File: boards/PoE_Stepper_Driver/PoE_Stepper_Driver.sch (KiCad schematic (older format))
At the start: 4 parts

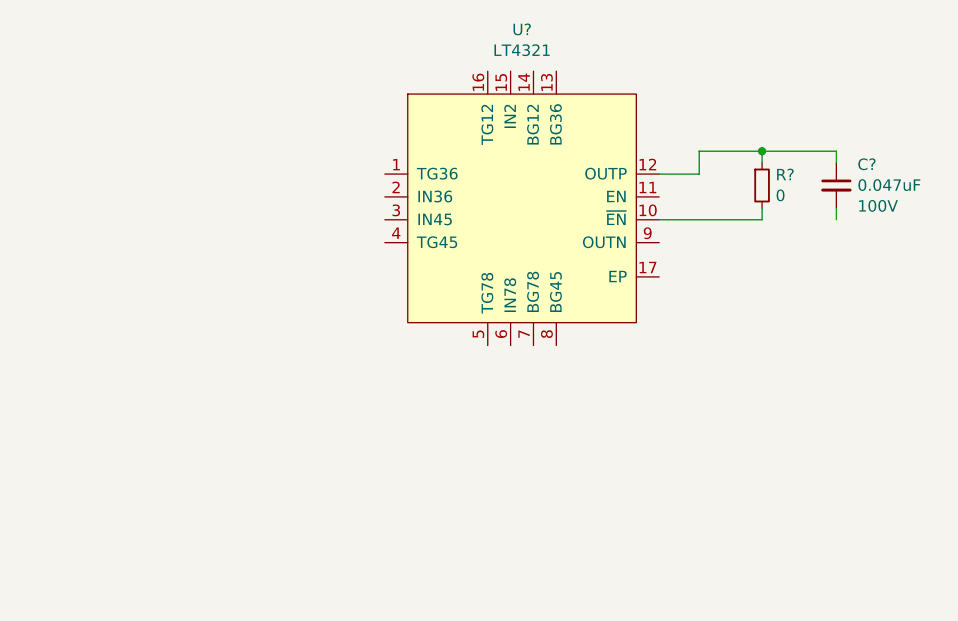
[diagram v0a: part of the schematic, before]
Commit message: started poe side of schematic
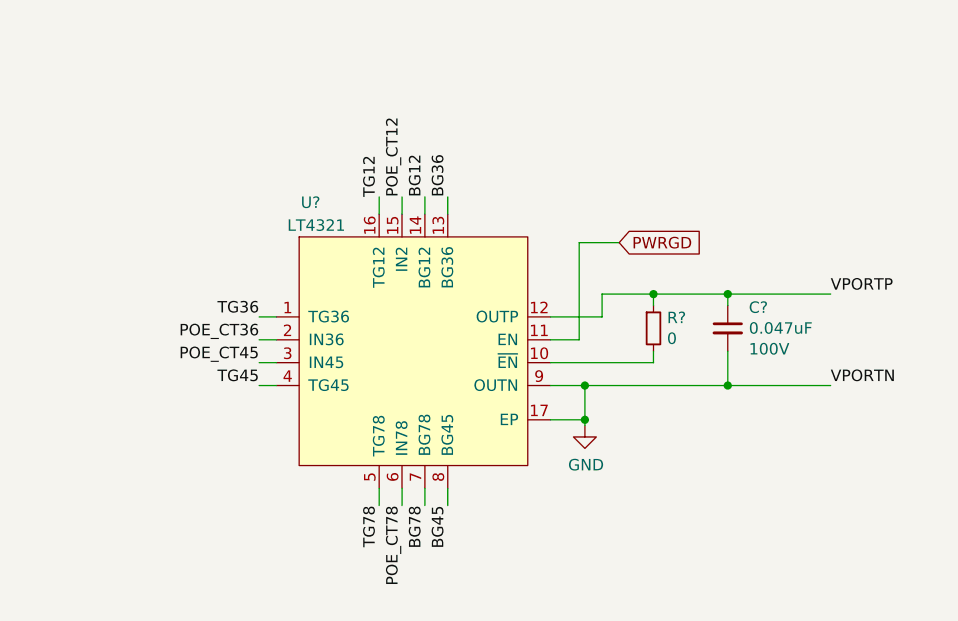
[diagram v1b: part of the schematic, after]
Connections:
- net labels added: BG12, BG36, BG45, BG78, GND, POE_CT12, POE_CT36, POE_CT45, POE_CT78, PWRGD, TG12, TG36, TG45, TG78, VPORTN, VPORTP
- wire segments 9 -> 31
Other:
- moved on the sheet: C?, R?, U?
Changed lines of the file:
@@
 L ECE445:LT4321 U?
 U 1 1 61FBDFD6
-P 6825 2875
-F 0 "U?" H 6825 3656 50  0000 C CNN
-F 1 "LT4321" H 6825 3565 50  0000 C CNN
-F 2 "" H 6475 3425 50  0001 C CNN
-F 3 "" H 6475 3425 50  0001 C CNN
-	1    6825 2875
+P 6350 3500
+F 0 "U?" H 5900 4150 50  0000 C CNN
+F 1 "LT4321" H 5925 4050 50  0000 C CNN
+F 2 "" H 6000 4050 50  0001 C CNN
+F 3 "" H 6000 4050 50  0001 C CNN
+	1    6350 3500
 	1    0    0    -1
 $EndComp
@@
 L device:C_Small C?
 U 1 1 61FBE7CA
-P 8200 2775
-F 0 "C?" H 8292 2866 50  0000 L CNN
-F 1 "0.047uF" H 8292 2775 50  0000 L CNN
-F 2 "" H 8200 2775 50  0001 C CNN
-F 3 "~" H 8200 2775 50  0001 C CNN
-F 4 "100V" H 8292 2684 50  0000 L CNN "Voltage"
-	1    8200 2775
+P 7725 3400
+F 0 "C?" H 7817 3491 50  0000 L CNN
+F 1 "0.047uF" H 7817 3400 50  0000 L CNN
+F 2 "" H 7725 3400 50  0001 C CNN
+F 3 "~" H 7725 3400 50  0001 C CNN
+F 4 "100V" H 7817 3309 50  0000 L CNN "Voltage"
+	1    7725 3400
 	1    0    0    -1
 $EndComp
 Wire Wire Line
-	8200 2625 8200 2675
-Wire Wire Line
-	8200 2925 8200 2875
+	7725 3250 7725 3300
 $Comp
 L device:R_Small R?
 U 1 1 61FC1A67
-P 7875 2775
-F 0 "R?" H 7934 2821 50  0000 L CNN
-F 1 "0" H 7934 2730 50  0000 L CNN
-F 2 "" H 7875 2775 50  0001 C CNN
-F 3 "~" H 7875 2775 50  0001 C CNN
-	1    7875 2775
+P 7400 3400
+F 0 "R?" H 7459 3446 50  0000 L CNN
+F 1 "0" H 7459 3355 50  0000 L CNN
+F 2 "" H 7400 3400 50  0001 C CNN
+F 3 "~" H 7400 3400 50  0001 C CNN
+	1    7400 3400
 	1    0    0    -1
 $EndComp
 Wire Wire Line
-	7875 2625 7875 2675
+	7400 3250 7400 3300
 Wire Wire Line
-	7875 2625 8200 2625
+	7400 3250 7725 3250
 Wire Wire Line
-	7875 2875 7875 2925
+	7400 3500 7400 3550
 Wire Wire Line
-	7875 2925 7425 2925
+	7400 3550 6950 3550
 Wire Wire Line
-	7425 2725 7600 2725
+	6950 3650 7100 3650
 Wire Wire Line
-	7600 2725 7600 2625
+	7725 3500 7725 3650
+Text GLabel 7250 3025 2    50   Input ~ 0
+PWRGD
 Wire Wire Line
-	7600 2625 7875 2625
-Connection ~ 7875 2625
+	6950 3450 7075 3450
+Wire Wire Line
+	7075 3450 7075 3025
+Wire Wire Line
+	7075 3025 7250 3025
+Wire Wire Line
+	7175 3350 7175 3250
+Wire Wire Line
+	7175 3250 7400 3250
+Wire Wire Line
+	6950 3350 7175 3350
+Connection ~ 7400 3250
+Text Label 6500 2825 1    50   ~ 0
+BG36
+Wire Wire Line
+	6500 2825 6500 2900
+Text Label 6400 2825 1    50   ~ 0
+BG12
+Wire Wire Line
+	6400 2825 6400 2900
+Text Label 6300 2825 1    50   ~ 0
+POE_CT12
+Wire Wire Line
+	6300 2825 6300 2900
+Text Label 6200 2825 1    50   ~ 0
+TG12
+Wire Wire Line
+	6200 2825 6200 2900
+Text Label 5675 3350 2    50   ~ 0
+TG36
+Wire Wire Line
+	5675 3350 5750 3350
+Text Label 5675 3450 2    50   ~ 0
+POE_CT36
+Wire Wire Line
+	5675 3450 5750 3450
+Text Label 5675 3550 2    50   ~ 0
+POE_CT45
+Wire Wire Line
+	5675 3550 5750 3550
+Text Label 5675 3650 2    50   ~ 0
+TG45
+Wire Wire Line
+	5675 3650 5750 3650
+Text Label 6200 4175 3    50   ~ 0
+TG78
+Wire Wire Line
+	6200 4175 6200 4100
+Text Label 6300 4175 3    50   ~ 0
+POE_CT78
+Wire Wire Line
+	6300 4175 6300 4100
+Text Label 6400 4175 3    50   ~ 0
+BG78
+Wire Wire Line
+	6400 4175 6400 4100
+Text Label 6500 4175 3    50   ~ 0
+BG45
+Wire Wire Line
+	6500 4175 6500 4100
+$Comp
+L power:GND #PWR?
+U 1 1 61FC94D9
+P 7100 3825
+F 0 "#PWR?" H 7100 3575 50  0001 C CNN
+F 1 "GND" H 7105 3652 50  0000 C CNN
+F 2 "" H 7100 3825 50  0001 C CNN
+F 3 "" H 7100 3825 50  0001 C CNN
+	1    7100 3825
+	1    0    0    -1
+$EndComp
+Wire Wire Line
+	6950 3800 7100 3800
+Wire Wire Line
+	7100 3800 7100 3825
+Wire Wire Line
+	7100 3650 7100 3800
+Connection ~ 7100 3650
+Wire Wire Line
+	7100 3650 7725 3650
+Connection ~ 7100 3800
+Text Label 8175 3250 0    50   ~ 0
+VPORTP
+Text Label 8175 3650 0    50   ~ 0
+VPORTN
+Wire Wire Line
+	7725 3250 8175 3250
+Connection ~ 7725 3250
+Wire Wire Line
+	7725 3650 8175 3650
+Connection ~ 7725 3650
 $EndSCHEMATC

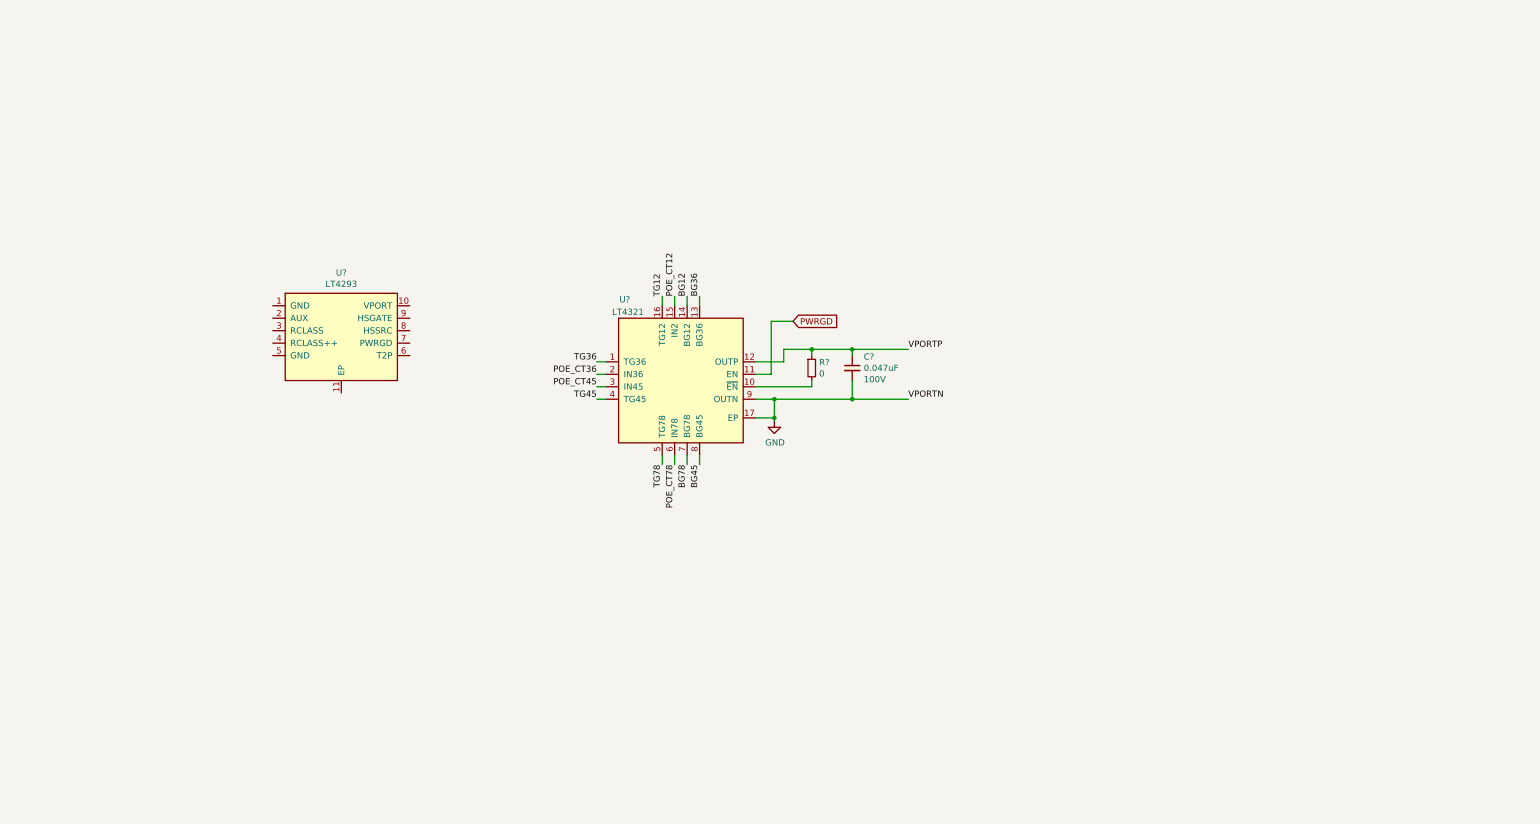
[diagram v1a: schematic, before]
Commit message: added ethernet transformer
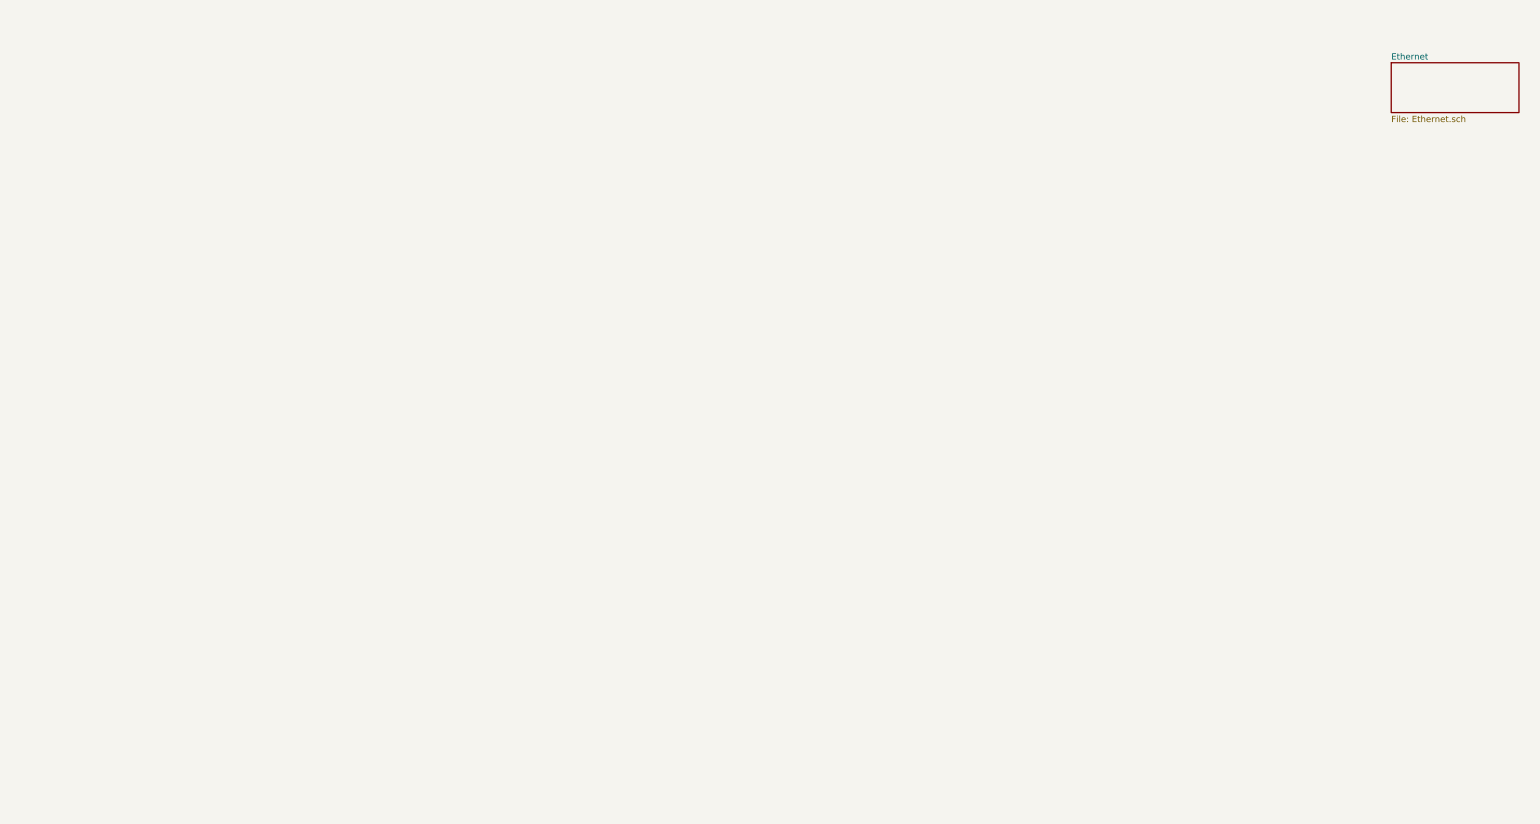
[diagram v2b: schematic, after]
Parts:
- removed C?: 0.047uF, symbol device:C_Small
- removed R?: 0, symbol device:R_Small
- removed U?: LT4293, symbol ECE445:LT4293
- removed U?: LT4321, symbol ECE445:LT4321
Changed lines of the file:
@@
 $Descr A4 11693 8268
 encoding utf-8
-Sheet 1 1
+Sheet 1 2
 Title ""
 Date ""
@@
 Comment4 ""
 $EndDescr
-$Comp
-L ECE445:LT4293 U?
-U 1 1 61FB857D
-P 3625 3100
-F 0 "U?" H 3625 3565 50  0000 C CNN
-F 1 "LT4293" H 3625 3474 50  0000 C CNN
-F 2 "" H 3475 3550 50  0001 C CNN
-F 3 "" H 3475 3550 50  0001 C CNN
-	1    3625 3100
-	1    0    0    -1
-$EndComp
-$Comp
-L ECE445:LT4321 U?
-U 1 1 61FBDFD6
-P 6350 3500
-F 0 "U?" H 5900 4150 50  0000 C CNN
-F 1 "LT4321" H 5925 4050 50  0000 C CNN
-F 2 "" H 6000 4050 50  0001 C CNN
-F 3 "" H 6000 4050 50  0001 C CNN
-	1    6350 3500
-	1    0    0    -1
-$EndComp
-$Comp
-L device:C_Small C?
-U 1 1 61FBE7CA
-P 7725 3400
-F 0 "C?" H 7817 3491 50  0000 L CNN
-F 1 "0.047uF" H 7817 3400 50  0000 L CNN
-F 2 "" H 7725 3400 50  0001 C CNN
-F 3 "~" H 7725 3400 50  0001 C CNN
-F 4 "100V" H 7817 3309 50  0000 L CNN "Voltage"
-	1    7725 3400
-	1    0    0    -1
-$EndComp
-Wire Wire Line
-	7725 3250 7725 3300
-$Comp
-L device:R_Small R?
-U 1 1 61FC1A67
-P 7400 3400
-F 0 "R?" H 7459 3446 50  0000 L CNN
-F 1 "0" H 7459 3355 50  0000 L CNN
-F 2 "" H 7400 3400 50  0001 C CNN
-F 3 "~" H 7400 3400 50  0001 C CNN
-	1    7400 3400
-	1    0    0    -1
-$EndComp
-Wire Wire Line
-	7400 3250 7400 3300
-Wire Wire Line
-	7400 3250 7725 3250
-Wire Wire Line
-	7400 3500 7400 3550
-Wire Wire Line
-	7400 3550 6950 3550
-Wire Wire Line
-	6950 3650 7100 3650
-Wire Wire Line
-	7725 3500 7725 3650
-Text GLabel 7250 3025 2    50   Input ~ 0
-PWRGD
-Wire Wire Line
-	6950 3450 7075 3450
-Wire Wire Line
-	7075 3450 7075 3025
-Wire Wire Line
-	7075 3025 7250 3025
-Wire Wire Line
-	7175 3350 7175 3250
-Wire Wire Line
-	7175 3250 7400 3250
-Wire Wire Line
-	6950 3350 7175 3350
-Connection ~ 7400 3250
-Text Label 6500 2825 1    50   ~ 0
-BG36
-Wire Wire Line
-	6500 2825 6500 2900
-Text Label 6400 2825 1    50   ~ 0
-BG12
-Wire Wire Line
-	6400 2825 6400 2900
-Text Label 6300 2825 1    50   ~ 0
-POE_CT12
-Wire Wire Line
-	6300 2825 6300 2900
-Text Label 6200 2825 1    50   ~ 0
-TG12
-Wire Wire Line
-	6200 2825 6200 2900
-Text Label 5675 3350 2    50   ~ 0
-TG36
-Wire Wire Line
-	5675 3350 5750 3350
-Text Label 5675 3450 2    50   ~ 0
-POE_CT36
-Wire Wire Line
-	5675 3450 5750 3450
-Text Label 5675 3550 2    50   ~ 0
-POE_CT45
-Wire Wire Line
-	5675 3550 5750 3550
-Text Label 5675 3650 2    50   ~ 0
-TG45
-Wire Wire Line
-	5675 3650 5750 3650
-Text Label 6200 4175 3    50   ~ 0
-TG78
-Wire Wire Line
-	6200 4175 6200 4100
-Text Label 6300 4175 3    50   ~ 0
-POE_CT78
-Wire Wire Line
-	6300 4175 6300 4100
-Text Label 6400 4175 3    50   ~ 0
-BG78
-Wire Wire Line
-	6400 4175 6400 4100
-Text Label 6500 4175 3    50   ~ 0
-BG45
-Wire Wire Line
-	6500 4175 6500 4100
-$Comp
-L power:GND #PWR?
-U 1 1 61FC94D9
-P 7100 3825
-F 0 "#PWR?" H 7100 3575 50  0001 C CNN
-F 1 "GND" H 7105 3652 50  0000 C CNN
-F 2 "" H 7100 3825 50  0001 C CNN
-F 3 "" H 7100 3825 50  0001 C CNN
-	1    7100 3825
-	1    0    0    -1
-$EndComp
-Wire Wire Line
-	6950 3800 7100 3800
-Wire Wire Line
-	7100 3800 7100 3825
-Wire Wire Line
-	7100 3650 7100 3800
-Connection ~ 7100 3650
-Wire Wire Line
-	7100 3650 7725 3650
-Connection ~ 7100 3800
-Text Label 8175 3250 0    50   ~ 0
-VPORTP
-Text Label 8175 3650 0    50   ~ 0
-VPORTN
-Wire Wire Line
-	7725 3250 8175 3250
-Connection ~ 7725 3250
-Wire Wire Line
-	7725 3650 8175 3650
-Connection ~ 7725 3650
+$Sheet
+S 12050 950  1025 400
+U 620ECB3C
+F0 "Ethernet" 50
+F1 "Ethernet.sch" 50
+$EndSheet
 $EndSCHEMATC

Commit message: added trinamic chips
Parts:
- added U?: STM32F107RBTx, Package_QFP:LQFP-64_10x10mm_P0.5mm, symbol MCU_ST_STM32F1:STM32F107RBTx
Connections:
- net labels added: PWRGD, VOUT+, VOUT-
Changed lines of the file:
@@
 $Descr A4 11693 8268
 encoding utf-8
-Sheet 1 2
+Sheet 1 3
 Title ""
 Date ""
@@
 F1 "Ethernet.sch" 50
 $EndSheet
+$Comp
+L MCU_ST_STM32F1:STM32F107RBTx U?
+U 1 1 6292DDC0
+P 6025 3225
+F 0 "U?" H 6025 1336 50  0000 C CNN
+F 1 "STM32F107RBTx" H 6025 1245 50  0000 C CNN
+F 2 "Package_QFP:LQFP-64_10x10mm_P0.5mm" H 5425 1525 50  0001 R CNN
+F 3 "http://www.st.com/st-web-ui/static/active/en/resource/technical/document/datasheet/CD00220364.pdf" H 6025 3225 50  0001 C CNN
+	1    6025 3225
+	1    0    0    -1
+$EndComp
+$Sheet
+S 12050 1575 1025 275
+U 6293177D
+F0 "Motor_Control" 50
+F1 "Motor_Control.sch" 50
+$EndSheet
+Text GLabel 1800 3575 0    50   Input ~ 0
+PWRGD
+Text GLabel 1800 3275 0    50   Input ~ 0
+VOUT+
+Text GLabel 1800 3425 0    50   Input ~ 0
+VOUT-
 $EndSCHEMATC

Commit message: pretty much finished motor subsystem schematic
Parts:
- removed U?: STM32F107RBTx, Package_QFP:LQFP-64_10x10mm_P0.5mm, symbol MCU_ST_STM32F1:STM32F107RBTx
- added C? (x2): 10uF, symbol device:CP1_Small
- added C? (x2): 0.1uF, symbol device:C_Small
- added C? (x2): C_Small, symbol device:C_Small
- added D?: LED_Small, symbol device:LED_Small
- added J?: Programming, symbol Connector:Conn_01x06_Male
- added R?: R_Small, symbol device:R_Small
- added U?: STM32F407VETx, Package_QFP:LQFP-100_14x14mm_P0.5mm, symbol MCU_ST_STM32F4:STM32F407VETx
- added U?: 12V DC/DC, Converter_DCDC:Converter_DCDC_Artesyn_ATA_SMD, symbol Converter_DCDC:ATA00A18S-L
- added U?: NCP1117, Package_TO_SOT_SMD:SOT-223-3_TabPin2, symbol Regulator_Linear:NCP1117-3.3_SOT223
- added Y?: 8MHz, symbol device:Crystal_Small
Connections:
- net labels added: +12V, +3V3, CLK_2660, CLK_429, GND, NSRT, SPI1_CS, SPI1_MISO, SPI1_MOSI, SPI1_SCK, SPI2_CS, SPI2_MISO, SPI2_MOSI, SPI2_SCK, SWCLK, SWDIO, SWO
- wire segments 0 -> 80
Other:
- note added: "Power"
